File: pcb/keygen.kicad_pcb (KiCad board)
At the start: 2 copper layers, 362.9 x 125.8 mm, 236 parts, among them J101 PJ-320A, J201 PJ-320A, SW101 =, SW102 1, SW103 2, SW104 3, SW105 4, SW106 5, SW107 Tab, SW108 Q, SW109 W, SW110 E, SW111 R, SW112 T, SW113 Esc, SW114 A, SW115 S, SW116 D, SW117 F, SW118 G, SW119 Alt, SW120 Shift, SW121 Z, SW122 X, SW123 C, SW124 V, SW125 B, SW126 Ctrl, SW127 `, SW128 Caps, SW129 Left, SW130 Right, SW131 Super, SW132 Bksp, SW133 Del, SW190 MSK12C02 power, SW191 Reset, SW201 -, SW202 0, SW203 9, SW204 8, SW205 7, SW206 6, SW208 \, SW209 P, SW210 O, SW211 I, SW212 U, SW213 Y, SW214 ', SW215 ;, SW216 L, SW217 K, SW218 J, SW219 H, SW220 Alt, SW221 Shift, SW222 /, SW223 ., SW224 ,, SW225 M, SW226 N, SW227 Ctrl, SW228 ], SW229 [, SW230 Down, SW231 Up, SW232 Fn, SW233 Space, SW234 Enter, SW290 MSK12C02 power, SW291 Reset, U101 nRF52840 Pro Micro, U201 nRF52840 Pro Micro

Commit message: Mark switch bodies on the front silkscreen
pcb/lib/keygen.pretty holds marbastlib's MX hotswap footprints with a
14 mm switch outline on B.SilkS, which lands on the front because the
footprints are placed flipped. Keeping it in a project library (instead
of editing placed footprints) avoids library-mismatch warnings and keeps
'update footprints from library' safe.
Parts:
- SW101, SW107, SW113, SW120, SW131, SW201, SW208, SW214, SW221, SW232: footprint marbastlib-mx:SW_MX_HS_CPG151101S11_1.25u -> keygen:SW_MX_HS_CPG151101S11_1.25u
- SW102, SW103, SW104, SW105, SW106, SW108, SW109, SW110, SW111, SW112, SW114, SW115, SW116, SW117, SW118, SW119, SW121, SW122, SW123, SW124, SW125, SW126, SW127, SW128, SW129, SW130, SW202, SW203, SW204, SW205, SW206, SW209, SW210, SW211, SW212, SW213, SW215, SW216, SW217, SW218, SW219, SW220, SW222, SW223, SW224, SW225, SW226, SW227, SW228, SW229, SW230, SW231: footprint marbastlib-mx:SW_MX_HS_CPG151101S11_1u -> keygen:SW_MX_HS_CPG151101S11_1u
- SW132, SW133, SW233, SW234: footprint marbastlib-mx:SW_MX_HS_CPG151101S11_1.5u -> keygen:SW_MX_HS_CPG151101S11_1.5u

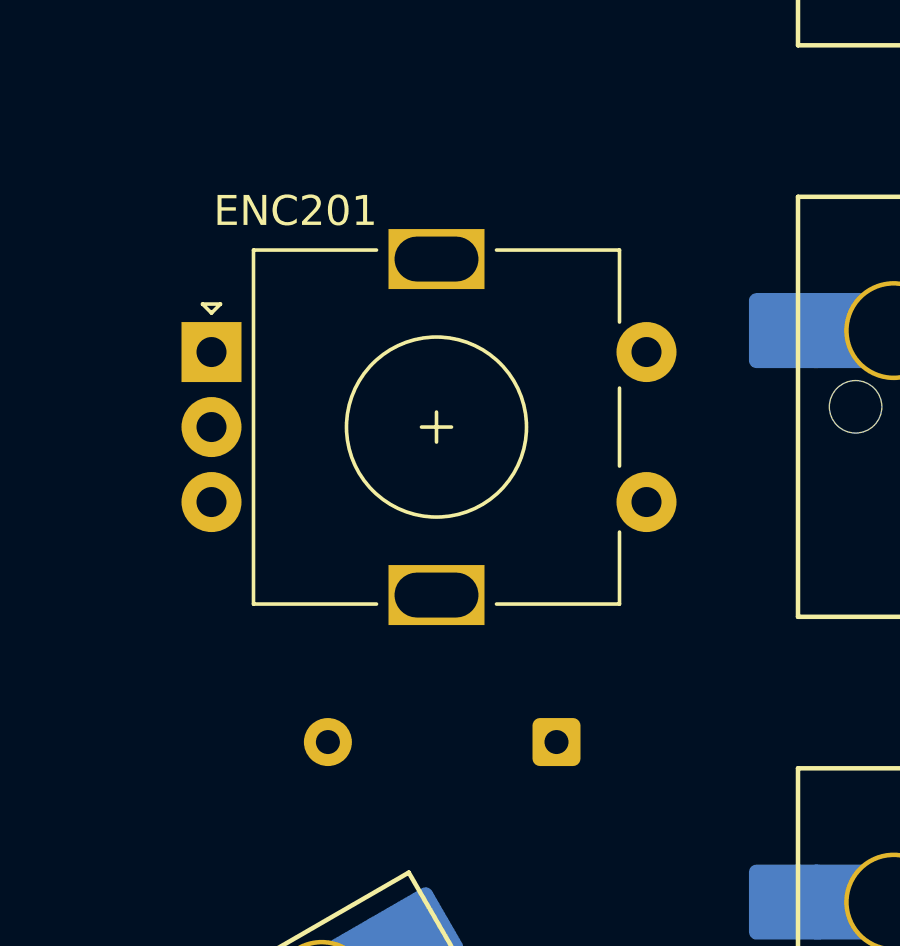
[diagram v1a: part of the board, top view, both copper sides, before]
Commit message: Show switches, keycaps and parts in KiCad's 3D view
Project copies of the vendored footprints point their 3D models inside
the repo. The hotswap footprints add a kiswitch MX switch and a generated
keycap, turned over so they stand on the front of a back-mounted part.
The controller gets a simple generated block. The encoder moves to
marbastlib's EC11 footprint (origin at the shaft) because KiCad's
encoder model isn't in the 3D package. Renders in docs/.
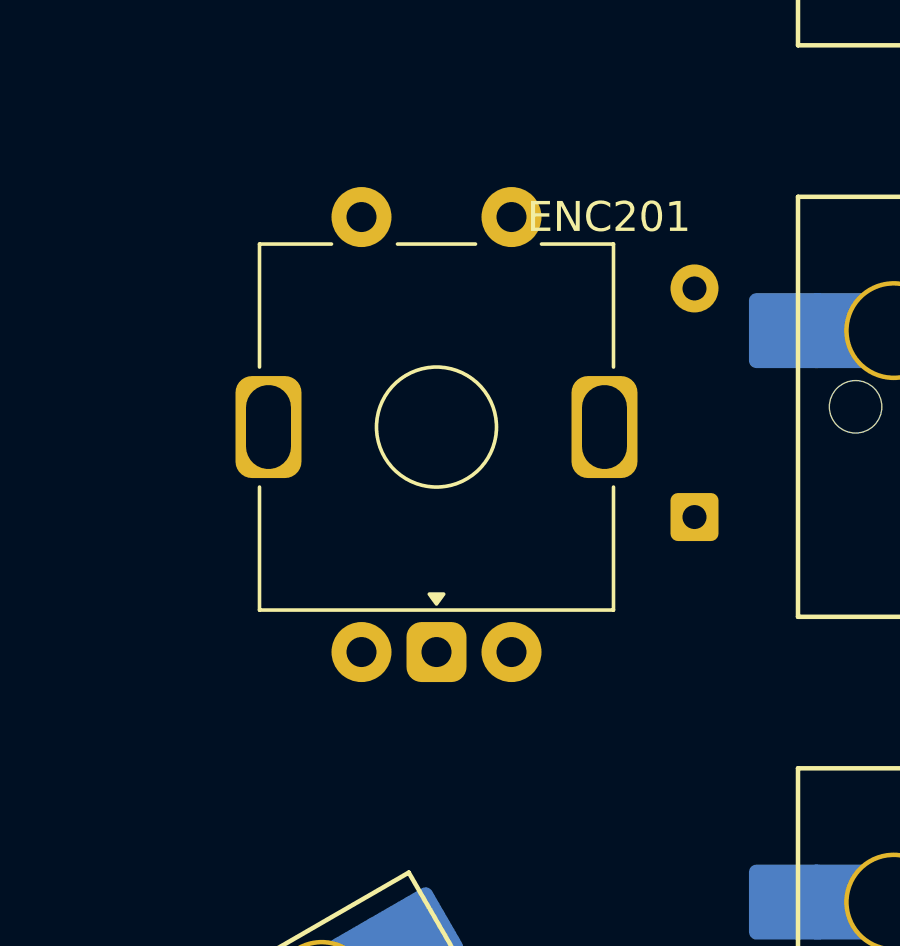
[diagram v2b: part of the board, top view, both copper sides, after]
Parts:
- ENC201: footprint Rotary_Encoder:RotaryEncoder_Alps_EC11E-Switch_Vertical_H20mm -> keygen:ROT_Alps_EC11E-Switch
- J101, J201: footprint Keebio-Parts:TRRS-PJ-320A -> keygen:TRRS-PJ-320A
- SW190, SW290: footprint marbastlib-various:SW_MSK12C02-HB -> keygen:SW_MSK12C02-HB
- U101, U201: footprint marbastlib-xp-promicroish:nice_nano_H_USBup -> keygen:nice_nano_H_USBup
- moved D207 8.80 mm to (261.7, 71.1), turned to 90 degrees
- moved ENC201 7.91 mm to (253.1, 68.1)

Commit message: Turn the tall thumb keys and put both halves on an A3 sheet
Redox's big thumb keys are 1 x 1.5u (tall), so their 1.5u footprints,
keycaps and LED/diode patterns rotate a quarter turn. The board moves to
the centre of an A3 drawing sheet with a filled title block (PAGE_INFO
isn't exposed to Python, so the generator sets the paper size in the
saved file). Also adds tools/route_pcb.py (Freerouting) for the next
step.
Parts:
- moved H203 168.8 mm to (258.0, 194.1)
- moved D234 74.1 mm to (256.9, 198.2), turned to 30 degrees
- moved D233 74.1 mm to (273.4, 188.7), turned to 30 degrees
- moved C101 62.0 mm to (36.2, 102.3)
- moved C102 62.0 mm to (39.7, 102.3)
- moved C201 62.0 mm to (374.3, 102.3)
- moved C202 62.0 mm to (377.8, 102.3)
- moved H103 62.0 mm to (182.3, 89.1)
- moved H105 62.0 mm to (53.8, 84.1)
- moved H205 62.0 mm to (371.0, 84.6)
- moved SW115 62.0 mm to (83.2, 126.0)
- moved SW117 62.0 mm to (121.2, 126.0)
- moved SW216 62.0 mm to (340.3, 126.0)
- moved SW218 62.0 mm to (302.2, 126.0)
- moved U101 62.0 mm to (159.3, 96.4)
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
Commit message: Route the PCB: DRC clean with schematic parity
Freerouting routes ~85% of signals with ground left to the pour; a grid
maze router (finish_route.py) completes the rest and ties stranded
ground pads to vias. Ground is poured on both layers per half with
stitching vias, islands removed and an antenna keep-out under each
controller. sync_pcb.py relinks footprints to the schematic; schematic
UUIDs are now deterministic so regenerating keeps those links, and the
generator no longer overwrites the project's design rules. Mounting
holes are in the schematic. Result: 0 unconnected, 0 errors, 0 parity
issues (28 silkscreen warnings remain).
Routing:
- net /right/VCC: track 0.00 -> 838.3 mm, vias 0 -> 29
- net /left/VCC: track 0.00 -> 798.4 mm, vias 0 -> 20
- net /left/COL0: track 0.00 -> 282.8 mm, vias 0 -> 1
- net /left/COL1: track 0.00 -> 231.2 mm, vias 0 -> 5
- net /left/ROW4: track 0.00 -> 230.5 mm, vias 0 -> 4
- net /right/ROW4: track 0.00 -> 228.2 mm, vias 0 -> 3
- net /right/COL1: track 0.00 -> 218.3 mm, vias 0 -> 9
- net /right/COL0: track 0.00 -> 211.8 mm, vias 0 -> 4
- net /right/ROW2: track 0.00 -> 201.6 mm, vias 0 -> 1
- net /left/GND: track 0.00 -> 200.5 mm, vias 0 -> 187
- net /left/ROW2: track 0.00 -> 199.7 mm
- net /left/COL2: track 0.00 -> 190.9 mm, vias 0 -> 7
- net /right/ROW0: track 0.00 -> 188.9 mm
- net /right/COL2: track 0.00 -> 182.5 mm, vias 0 -> 3
- net /left/ROW3: track 0.00 -> 182.1 mm, vias 0 -> 1
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- added copper zone on B.Cu, net /left/GND
- added copper zone on F.Cu, net /left/GND
- added copper zone on B.Cu, net /right/GND
- added copper zone on F.Cu, net /right/GND
